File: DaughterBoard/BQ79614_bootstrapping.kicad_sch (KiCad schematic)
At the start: 5 parts, among them U1 BQ79614PAPRQ1

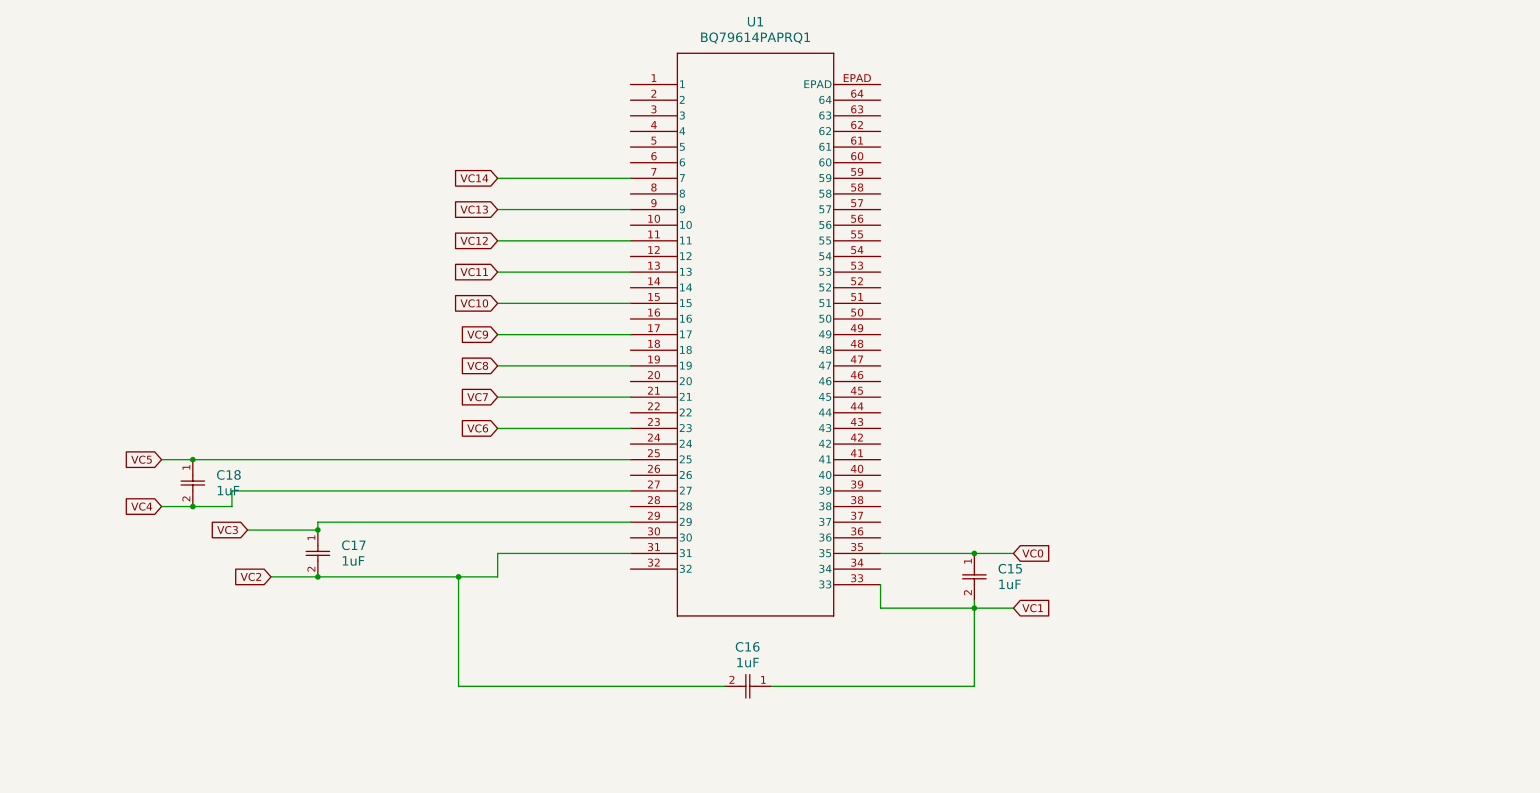
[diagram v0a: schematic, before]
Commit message: Add files via upload
Updated KiCAD schematics for Daughter Board. (10/10/24)
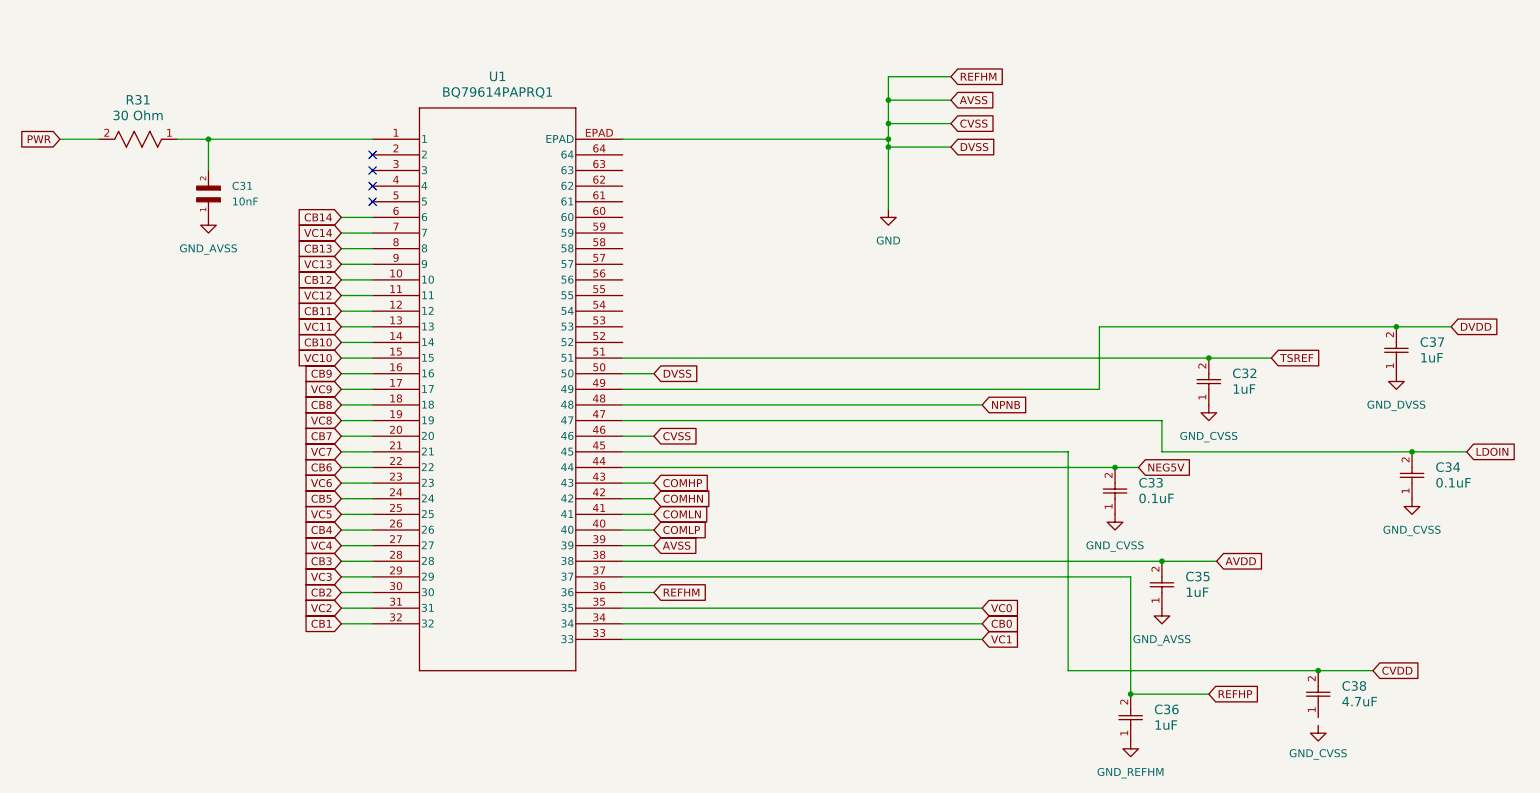
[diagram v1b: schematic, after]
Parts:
- removed C15, C16, C17, C18: 1uF, YAG_CC0603_YAG, symbol 2024-10-01_14-56-27:CC0603KRX7R7BB105
- added C31: 10nF, GCM188R72A103KA37J:CAPC1608X90N, symbol GCM188R72A103KA37J:GCM188R72A103KA37J
- added C32, C35, C36, C37: 1uF, C0603C105K8RACAUTO:CAPC18095_95N_KEM-L, symbol C0603C105K8RACAUTO:C0603C105K8RACAUTO
- added C33, C34: 0.1uF, GCM155R71A104KA55D:CAP_GCM15_1p05X0p55X0p55_MUR-L, symbol GCM155R71A104KA55D:GCM155R71A104KA55D
- added C38: 4.7uF, C2012X7R1A475M125AC:CAP_2012_TDK-L, symbol C2012X7R1A475M125AC:C2012X7R1A475M125AC
- added R31: 30 Ohm, ERJ-3EKF30R0V:RC0603N_PAN, symbol 2024-10-08_19-57-08:ERJ-3EKF30R0V
- U1: footprint QFP_4PAPRQ1_TEX -> BQ79614:QFP_4PAPRQ1_TEX-L
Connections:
- net at U1.1: now also C31.2, R31.1
- net CB12: now reaches U1.10
- net CB11: now reaches U1.12
- net CB10: now reaches U1.14
- net CB9: now reaches U1.16
- net CB8: now reaches U1.18
- net CB7: now reaches U1.20
- net CB6: now reaches U1.22
- net CB5: now reaches U1.24
- net CB4: now reaches U1.26
- net CB3: now reaches U1.28
- net CB2: now reaches U1.30
- net CB1: now reaches U1.32
- net CB0: now reaches U1.34
- net GND: now reaches U1.36
- net GND: now also U1.39, U1.46, U1.50, U1.EPAD
- net REFHP: now reaches U1.37
- net REFHP: now also C36.2
- net AVDD: now reaches U1.38
- net AVDD: now also C35.2
- net COMLP: now reaches U1.40
- net COMLN: now reaches U1.41
- net COMHN: now reaches U1.42
- net COMHP: now reaches U1.43
- net NEG5V: now reaches U1.44
- net NEG5V: now also C33.2
- net CVDD: now reaches U1.45
- net CVDD: now also C38.2
- net LDOIN: now reaches U1.47
- net LDOIN: now also C34.2
- net NPNB: now reaches U1.48
- net DVDD: now reaches U1.49
- net DVDD: now also C37.2
- net TSREF: now reaches U1.51
- net TSREF: now also C32.2
- net CB14: now reaches U1.6
- net CB13: now reaches U1.8
- new net GND_AVSS: C31.1, C35.1
- new net GND_CVSS: C32.1, C33.1, C34.1
- new net GND_DVSS: C37.1
- new net GND_REFHM: C36.1
- new net PWR: R31.2
- no-connect marks 0 -> 4
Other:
- title: (none) -> BQ79614 Peripheral
- moved on the sheet: U1

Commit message: modhy commit
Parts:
- renumbered C31 to C1, C33 to C2, C36 to C3, C35 to C4, C32 to C5, C38 to C6, C37 to C7, C34 to C8, R31 to R1
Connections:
- net CVDD: now also U1.52
- net GND_CVSS: now also C6.1
- net BBN: now reaches U1.63
- net BBP: now reaches U1.64
- no-connect marks 4 -> 13
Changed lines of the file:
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@@
 	)
 	(no_connect
+		(at 135.89 67.31)
+	)
+	(no_connect
+		(at 135.89 77.47)
+	)
+	(no_connect
+		(at 135.89 74.93)
+	)
+	(no_connect
 		(at 95.25 52.07)
 	)
 	(no_connect
+		(at 135.89 64.77)
+	)
+	(no_connect
+		(at 135.89 62.23)
+	)
+	(no_connect
+		(at 135.89 72.39)
+	)
+	(no_connect
+		(at 135.89 69.85)
+	)
+	(no_connect
+		(at 135.89 57.15)
+	)
+	(no_connect
+		(at 135.89 59.69)
+	)
+	(no_connect
 		(at 95.25 59.69)
 	)
@@
 		(at 95.25 57.15)
 	)
+	(bus_entry
+		(at 172.72 52.07)
+		(size 2.54 2.54)
+		(stroke
+			(width 0)
+			(type default)
+		)
+	)
+	(bus_entry
+		(at 172.72 54.61)
+		(size 2.54 2.54)
+		(stroke
+			(width 0)
+			(type default)
+		)
+	)
 	(wire
 		(pts
@@
 		)
 	)
+	(bus
+		(pts
+			(xy 175.26 54.61) (xy 175.26 57.15)
+		)
+		(stroke
+			(width 0)
+			(type default)
+		)
+	)
 	(wire
 		(pts
@@
 	(wire
 		(pts
+			(xy 135.89 82.55) (xy 140.97 82.55)
+		)
+		(stroke
+			(width 0)
+			(type default)
+		)
+	)
+	(wire
+		(pts
 			(xy 223.52 118.11) (xy 232.41 118.11)
 		)
@@
 	(wire
 		(pts
+			(xy 135.89 54.61) (xy 172.72 54.61)
+		)
+		(stroke
+			(width 0)
+			(type default)
+		)
+	)
+	(wire
+		(pts
 			(xy 90.17 97.79) (xy 95.25 97.79)
 		)
@@
 	(wire
 		(pts
+			(xy 135.89 52.07) (xy 172.72 52.07)
+		)
+		(stroke
+			(width 0)
+			(type default)
+		)
+	)
+	(wire
+		(pts
 			(xy 135.89 87.63) (xy 140.97 87.63)
 		)
@@
 		)
 	)
+	(label "BBP"
+		(at 172.72 52.07 0)
+		(fields_autoplaced yes)
+		(effects
+			(font
+				(size 1.27 1.27)
+			)
+			(justify left bottom)
+		)
+	)
+	(label "BBN"
+		(at 172.72 54.61 0)
+		(fields_autoplaced yes)
+		(effects
+			(font
+				(size 1.27 1.27)
+			)
+			(justify left bottom)
+		)
+	)
 	(global_label "NEG5V"
 		(shape input)
@@
 		)
 	)
+	(global_label "CVDD"
+		(shape input)
+		(at 140.97 82.55 0)
+		(fields_autoplaced yes)
+		(effects
+			(font
+				(size 1.27 1.27)
+			)
+			(justify left)
+		)
+		(property "Intersheetrefs" "${INTERSHEET_REFS}"
+			(at 148.8538 82.55 0)
+			(effects
+				(font
+					(size 1.27 1.27)
+				)
+				(justify left)
+				(hide yes)
+			)
+		)
+	)
 	(global_label "CB14"
 		(shape input)
@@
 		(dnp no)
 		(fields_autoplaced yes)
-		(property "Reference" "C32"
+		(property "Reference" "C5"
 			(at 234.95 87.6299 90)
 			(effects
@@
 			(project "Project63_BMS_DaughterBoard"
 				(path "/325b096d-8e4c-4cdc-b4c5-634ea5e73c60/8ffa0956-e90f-44b3-af43-d8470a47be31"
-					(reference "C32")
+					(reference "C5")
 					(unit 1)
 				)
@@
 		(dnp no)
 		(fields_autoplaced yes)
-		(property "Reference" "C33"
+		(property "Reference" "C2"
 			(at 219.71 105.4099 90)
 			(effects
@@
 			(project "Project63_BMS_DaughterBoard"
 				(path "/325b096d-8e4c-4cdc-b4c5-634ea5e73c60/8ffa0956-e90f-44b3-af43-d8470a47be31"
-					(reference "C33")
+					(reference "C2")
 					(unit 1)
 				)
@@
 	(symbol
 		(lib_id "power:GND1")
-		(at 248.92 144.78 0)
+		(at 248.92 143.51 0)
 		(unit 1)
 		(exclude_from_sim no)
@@
 		(on_board yes)
 		(dnp no)
-		(property "Reference" "#PWR010"
-			(at 248.92 151.13 0)
+		(property "Reference" "#PWR0101"
+			(at 248.92 149.86 0)
 			(effects
 				(font
@@
 		)
 		(property "Value" "GND_CVSS"
-			(at 248.92 149.352 0)
+			(at 248.92 148.082 0)
 			(effects
 				(font
@@
 		)
 		(property "Footprint" ""
-			(at 248.92 144.78 0)
+			(at 248.92 143.51 0)
 			(effects
 				(font
@@
 		)
 		(property "Datasheet" ""
-			(at 248.92 144.78 0)
+			(at 248.92 143.51 0)
 			(effects
 				(font
@@
 		)
 		(property "Description" "Power symbol creates a global label with name \"GND1\" , ground"
-			(at 248.92 144.78 0)
+			(at 248.92 143.51 0)
 			(effects
 				(font
@@
 			(project "Project63_BMS_DaughterBoard"
 				(path "/325b096d-8e4c-4cdc-b4c5-634ea5e73c60/8ffa0956-e90f-44b3-af43-d8470a47be31"
-					(reference "#PWR010")
+					(reference "#PWR0101")
 					(unit 1)
 				)
@@
 		(dnp no)
 		(fields_autoplaced yes)
-		(property "Reference" "#PWR09"
+		(property "Reference" "#PWR0102"
 			(at 261.62 93.98 0)
 			(effects
@@
 			(project "Project63_BMS_DaughterBoard"
 				(path "/325b096d-8e4c-4cdc-b4c5-634ea5e73c60/8ffa0956-e90f-44b3-af43-d8470a47be31"
-					(reference "#PWR09")
+					(reference "#PWR0102")
 					(unit 1)
 				)
@@
 		(dnp no)
 		(fields_autoplaced yes)
-		(property "Reference" "C35"
+		(property "Reference" "C4"
 			(at 227.33 120.6499 90)
 			(effects
@@
 			(project "Project63_BMS_DaughterBoard"
 				(path "/325b096d-8e4c-4cdc-b4c5-634ea5e73c60/8ffa0956-e90f-44b3-af43-d8470a47be31"
-					(reference "C35")
+					(reference "C4")
 					(unit 1)
 				)
@@
 		(dnp no)
 		(fields_autoplaced yes)
-		(property "Reference" "#PWR06"
+		(property "Reference" "#PWR0106"
 			(at 264.16 114.3 0)
 			(effects
@@
 			(project "Project63_BMS_DaughterBoard"
 				(path "/325b096d-8e4c-4cdc-b4c5-634ea5e73c60/8ffa0956-e90f-44b3-af43-d8470a47be31"
-					(reference "#PWR06")
+					(reference "#PWR0106")
 					(unit 1)
 				)
@@
 		(dnp no)
 		(fields_autoplaced yes)
-		(property "Reference" "C31"
+		(property "Reference" "C1"
 			(at 72.39 57.1499 90)
 			(effects
@@
 			(project "Project63_BMS_DaughterBoard"
 				(path "/325b096d-8e4c-4cdc-b4c5-634ea5e73c60/8ffa0956-e90f-44b3-af43-d8470a47be31"
-					(reference "C31")
+					(reference "C1")
 					(unit 1)
 				)
@@
 		(dnp no)
 		(fields_autoplaced yes)
-		(property "Reference" "R31"
+		(property "Reference" "R1"
 			(at 57.15 43.18 0)
 			(effects
@@
 			(project "Project63_BMS_DaughterBoard"
 				(path "/325b096d-8e4c-4cdc-b4c5-634ea5e73c60/8ffa0956-e90f-44b3-af43-d8470a47be31"
-					(reference "R31")
+					(reference "R1")
 					(unit 1)
 				)
@@
 		(dnp no)
 		(fields_autoplaced yes)
-		(property "Reference" "C34"
+		(property "Reference" "C8"
 			(at 267.97 102.8699 90)
 			(effects
@@
 			(project "Project63_BMS_DaughterBoard"
 				(path "/325b096d-8e4c-4cdc-b4c5-634ea5e73c60/8ffa0956-e90f-44b3-af43-d8470a47be31"
-					(reference "C34")
+					(reference "C8")
 					(unit 1)
 				)
@@
 		(dnp no)
 		(fields_autoplaced yes)
-		(property "Reference" "#PWR01"
+		(property "Reference" "#PWR0109"
 			(at 68.58 68.58 0)
 			(effects
@@
 			(project "Project63_BMS_DaughterBoard"
 				(path "/325b096d-8e4c-4cdc-b4c5-634ea5e73c60/8ffa0956-e90f-44b3-af43-d8470a47be31"
-					(reference "#PWR01")
+					(reference "#PWR0109")
 					(unit 1)
 				)
@@
 		(dnp no)
 		(fields_autoplaced yes)
-		(property "Reference" "#PWR07"
+		(property "Reference" "#PWR0105"
 			(at 223.52 132.08 0)
 			(effects
@@
 			(project "Project63_BMS_DaughterBoard"
 				(path "/325b096d-8e4c-4cdc-b4c5-634ea5e73c60/8ffa0956-e90f-44b3-af43-d8470a47be31"
-					(reference "#PWR07")
+					(reference "#PWR0105")
 					(unit 1)
 				)
@@
 		(dnp no)
 		(fields_autoplaced yes)
-		(property "Reference" "#PWR04"
+		(property "Reference" "#PWR0104"
 			(at 231.14 99.06 0)
 			(effects
@@
 			(project "Project63_BMS_DaughterBoard"
 				(path "/325b096d-8e4c-4cdc-b4c5-634ea5e73c60/8ffa0956-e90f-44b3-af43-d8470a47be31"
-					(reference "#PWR04")
+					(reference "#PWR0104")
 					(unit 1)
 				)
@@
 		(dnp no)
 		(fields_autoplaced yes)
-		(property "Reference" "C37"
+		(property "Reference" "C7"
 			(at 265.43 82.5499 90)
 			(effects
@@
 			(project "Project63_BMS_DaughterBoard"
 				(path "/325b096d-8e4c-4cdc-b4c5-634ea5e73c60/8ffa0956-e90f-44b3-af43-d8470a47be31"
-					(reference "C37")
+					(reference "C7")
 					(unit 1)
 				)
@@
 		(dnp no)
 		(fields_autoplaced yes)
-		(property "Reference" "#PWR011"
+		(property "Reference" "#PWR0108"
 			(at 179.07 67.31 0)
 			(effects
@@
 			(project "Project63_BMS_DaughterBoard"
 				(path "/325b096d-8e4c-4cdc-b4c5-634ea5e73c60/8ffa0956-e90f-44b3-af43-d8470a47be31"
-					(reference "#PWR011")
+					(reference "#PWR0108")
 					(unit 1)
 				)
@@
 		(dnp no)
 		(fields_autoplaced yes)
-		(property "Reference" "#PWR05"
+		(property "Reference" "#PWR0103"
 			(at 215.9 116.84 0)
 			(effects
@@
 			(project "Project63_BMS_DaughterBoard"
 				(path "/325b096d-8e4c-4cdc-b4c5-634ea5e73c60/8ffa0956-e90f-44b3-af43-d8470a47be31"
-					(reference "#PWR05")
+					(reference "#PWR0103")
 					(unit 1)
 				)
@@
 		(dnp no)
 		(fields_autoplaced yes)
-		(property "Reference" "#PWR08"
+		(property "Reference" "#PWR0107"
 			(at 218.44 153.67 0)
 			(effects
@@
 			(project "Project63_BMS_DaughterBoard"
 				(path "/325b096d-8e4c-4cdc-b4c5-634ea5e73c60/8ffa0956-e90f-44b3-af43-d8470a47be31"
-					(reference "#PWR08")
+					(reference "#PWR0107")
 					(unit 1)
 				)
@@
 		(dnp no)
 		(fields_autoplaced yes)
-		(property "Reference" "C36"
+		(property "Reference" "C3"
 			(at 222.25 142.2399 90)
 			(effects
@@
 			(project "Project63_BMS_DaughterBoard"
 				(path "/325b096d-8e4c-4cdc-b4c5-634ea5e73c60/8ffa0956-e90f-44b3-af43-d8470a47be31"
-					(reference "C36")
+					(reference "C3")
 					(unit 1)
 				)
@@
 		(dnp no)
 		(fields_autoplaced yes)
-		(property "Reference" "C38"
+		(property "Reference" "C6"
 			(at 252.73 138.4299 90)
 			(effects
@@
 			(project "Project63_BMS_DaughterBoard"
 				(path "/325b096d-8e4c-4cdc-b4c5-634ea5e73c60/8ffa0956-e90f-44b3-af43-d8470a47be31"
-					(reference "C38")
+					(reference "C6")
 					(unit 1)
 				)

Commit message: 90% DOBO is done
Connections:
- net BBN: no longer names the net of U1.63
- net BBP: no longer names the net of U1.64
- no-connect marks 13 -> 16
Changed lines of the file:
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@@
+	)
+	(no_connect
+		(at 135.89 52.07)
 	)
 	(no_connect
@@
 	)
 	(no_connect
+		(at 135.89 54.61)
+	)
+	(no_connect
 		(at 135.89 62.23)
 	)
@@
 	)
 	(no_connect
+		(at 135.89 80.01)
+	)
+	(no_connect
 		(at 135.89 59.69)
 	)
@@
 		(at 95.25 57.15)
 	)
-	(bus_entry
-		(at 172.72 52.07)
-		(size 2.54 2.54)
-		(stroke
-			(width 0)
-			(type default)
-		)
-	)
-	(bus_entry
-		(at 172.72 54.61)
-		(size 2.54 2.54)
-		(stroke
-			(width 0)
-			(type default)
-		)
-	)
 	(wire
 		(pts
@@
 		)
 	)
-	(bus
-		(pts
-			(xy 175.26 54.61) (xy 175.26 57.15)
-		)
-		(stroke
-			(width 0)
-			(type default)
-		)
-	)
 	(wire
 		(pts
@@
 	(wire
 		(pts
-			(xy 135.89 54.61) (xy 172.72 54.61)
-		)
-		(stroke
-			(width 0)
-			(type default)
-		)
-	)
-	(wire
-		(pts
 			(xy 90.17 97.79) (xy 95.25 97.79)
 		)
@@
 	(wire
 		(pts
-			(xy 135.89 52.07) (xy 172.72 52.07)
-		)
-		(stroke
-			(width 0)
-			(type default)
-		)
-	)
-	(wire
-		(pts
 			(xy 135.89 87.63) (xy 140.97 87.63)
 		)
@@
 		)
 	)
-	(label "BBP"
-		(at 172.72 52.07 0)
-		(fields_autoplaced yes)
-		(effects
-			(font
-				(size 1.27 1.27)
-			)
-			(justify left bottom)
-		)
-	)
-	(label "BBN"
-		(at 172.72 54.61 0)
-		(fields_autoplaced yes)
-		(effects
-			(font
-				(size 1.27 1.27)
-			)
-			(justify left bottom)
-		)
-	)
